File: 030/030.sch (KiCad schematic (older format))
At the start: 7 parts, among them J1 Conn_01x12, J2 USB_C_Receptacle_USB2.0

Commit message: update 030 to potentially correct schematic. Remove bad 001/011.
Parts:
- removed R3, R4: comp, Resistor_SMD:R_0603_1608Metric_Pad0.98x0.95mm_HandSolder, symbol Device:R
- D1: symbol MSL0104RGB:MSL0104RGB -> 030-rescue:MSL0104RGB-MSL0104RGB
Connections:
- net +5V: now also J1.5 (Pin_5), J1.6 (Pin_6); no longer D1.1 (R_Annode), D1.2 (G_Annode), D1.6 (B_Annode), D1.7 (R_Annode), J1.8 (Pin_8)
- net D+: now also J2.A6 (D+), J2.B6 (D+)
- net D-: now also J2.A7 (D-), J2.B7 (D-)
- new net Annode: D1.1 (R_Annode), D1.2 (G_Annode), D1.6 (B_Annode), D1.7 (R_Annode), J1.8 (Pin_8)
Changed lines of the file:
@@
 	2300 2150 2250 2150
 Connection ~ 2250 2150
-Text Label 1750 2150 3    50   ~ 0
-D+
-Text Label 1950 2150 3    50   ~ 0
-D-
 $Comp
 L power:+5V #PWR0104
@@
 L power:+5V #PWR0109
 U 1 1 62279281
-P 900 2400
-F 0 "#PWR0109" H 900 2250 50  0001 C CNN
-F 1 "+5V" V 915 2528 50  0000 L CNN
-F 2 "" H 900 2400 50  0001 C CNN
-F 3 "" H 900 2400 50  0001 C CNN
-	1    900  2400
+P 900 2650
+F 0 "#PWR0109" H 900 2500 50  0001 C CNN
+F 1 "+5V" V 915 2778 50  0000 L CNN
+F 2 "" H 900 2650 50  0001 C CNN
+F 3 "" H 900 2650 50  0001 C CNN
+	1    900  2650
 	0    1    1    0
 $EndComp
 Wire Wire Line
-	900  2600 900  2700
+	900  2600 900  2650
 Text Label 900  3000 0    50   ~ 0
 D+
@@
 Text Label 900  2100 0    50   ~ 0
 B
+Connection ~ 900  2650
+Wire Wire Line
+	900  2650 900  2700
+Text Label 900  2400 0    50   ~ 0
+Annode
+Text Label 2100 3050 1    50   ~ 0
+Annode
+Text Label 1600 3050 1    50   ~ 0
+Annode
+Text Label 1500 3050 1    50   ~ 0
+Annode
 $Comp
-L MSL0104RGB:MSL0104RGB D1
+L 030-rescue:MSL0104RGB-MSL0104RGB D1
 U 1 1 6226D102
 P 1800 3200
@@
 	-1   0    0    1
 $EndComp
-$Comp
-L power:+5V #PWR0110
-U 1 1 6226E87F
-P 1500 3050
-F 0 "#PWR0110" H 1500 2900 50  0001 C CNN
-F 1 "+5V" H 1515 3223 50  0000 C CNN
-F 2 "" H 1500 3050 50  0001 C CNN
-F 3 "" H 1500 3050 50  0001 C CNN
-	1    1500 3050
-	1    0    0    -1
-$EndComp
-$Comp
-L power:+5V #PWR0111
-U 1 1 6226F068
-P 2100 3050
-F 0 "#PWR0111" H 2100 2900 50  0001 C CNN
-F 1 "+5V" H 2115 3223 50  0000 C CNN
-F 2 "" H 2100 3050 50  0001 C CNN
-F 3 "" H 2100 3050 50  0001 C CNN
-	1    2100 3050
-	1    0    0    -1
-$EndComp
-$Comp
-L power:+5V #PWR0112
-U 1 1 6226F88D
-P 1600 3050
-F 0 "#PWR0112" H 1600 2900 50  0001 C CNN
-F 1 "+5V" H 1615 3223 50  0000 C CNN
-F 2 "" H 1600 3050 50  0001 C CNN
-F 3 "" H 1600 3050 50  0001 C CNN
-	1    1600 3050
-	1    0    0    -1
-$EndComp
-$Comp
-L power:+5V #PWR0113
-U 1 1 6226FB45
-P 2000 3050
-F 0 "#PWR0113" H 2000 2900 50  0001 C CNN
-F 1 "+5V" H 2015 3223 50  0000 C CNN
-F 2 "" H 2000 3050 50  0001 C CNN
-F 3 "" H 2000 3050 50  0001 C CNN
-	1    2000 3050
-	1    0    0    -1
-$EndComp
-Text Label 1700 3050 0    50   ~ 0
+Text Label 2000 3050 1    50   ~ 0
+Annode
+Text Label 1800 3050 1    50   ~ 0
+R
+Text Label 1700 3050 1    50   ~ 0
 B
-Text Label 1800 3050 0    50   ~ 0
-R
-Text Label 1900 3050 0    50   ~ 0
+Text Label 1750 1850 3    50   ~ 0
+D+
+Text Label 1950 1850 3    50   ~ 0
+D-
+Text Label 1900 3050 1    50   ~ 0
 G
-$Comp
-L Device:R R3
-U 1 1 62270907
-P 1750 2000
-F 0 "R3" V 1650 1950 50  0000 L CNN
-F 1 "comp" V 1750 1900 50  0000 L CNN
-F 2 "Resistor_SMD:R_0603_1608Metric_Pad0.98x0.95mm_HandSolder" V 1680 2000 50  0001 C CNN
-F 3 "~" H 1750 2000 50  0001 C CNN
-	1    1750 2000
-	1    0    0    -1
-$EndComp
-$Comp
-L Device:R R4
-U 1 1 62270BB0
-P 1950 2000
-F 0 "R4" V 1850 1950 50  0000 L CNN
-F 1 "comp" V 1950 1900 50  0000 L CNN
-F 2 "Resistor_SMD:R_0603_1608Metric_Pad0.98x0.95mm_HandSolder" V 1880 2000 50  0001 C CNN
-F 3 "~" H 1950 2000 50  0001 C CNN
-	1    1950 2000
-	1    0    0    -1
-$EndComp
 $EndSCHEMATC

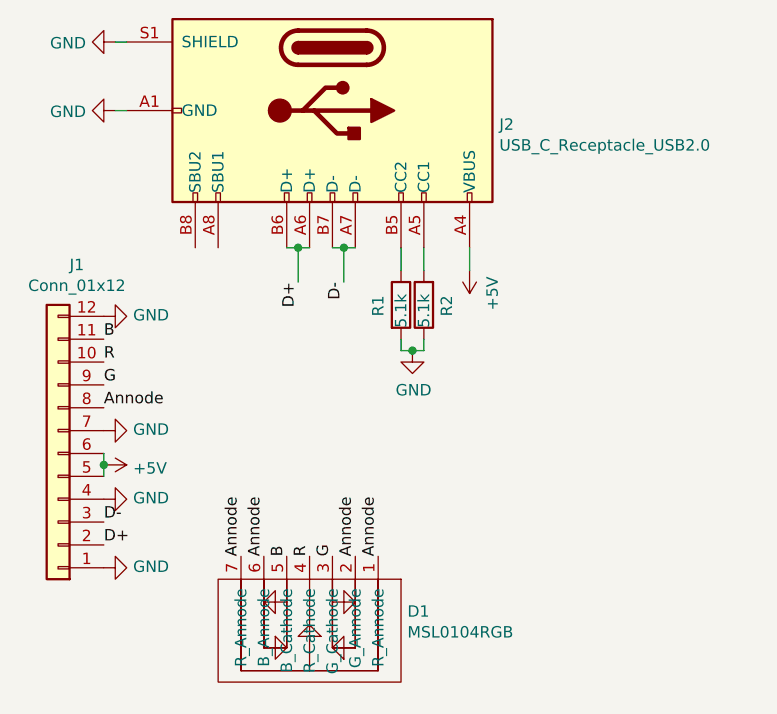
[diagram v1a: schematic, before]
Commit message: 001, 011, 030 standardized to a cheaper LED
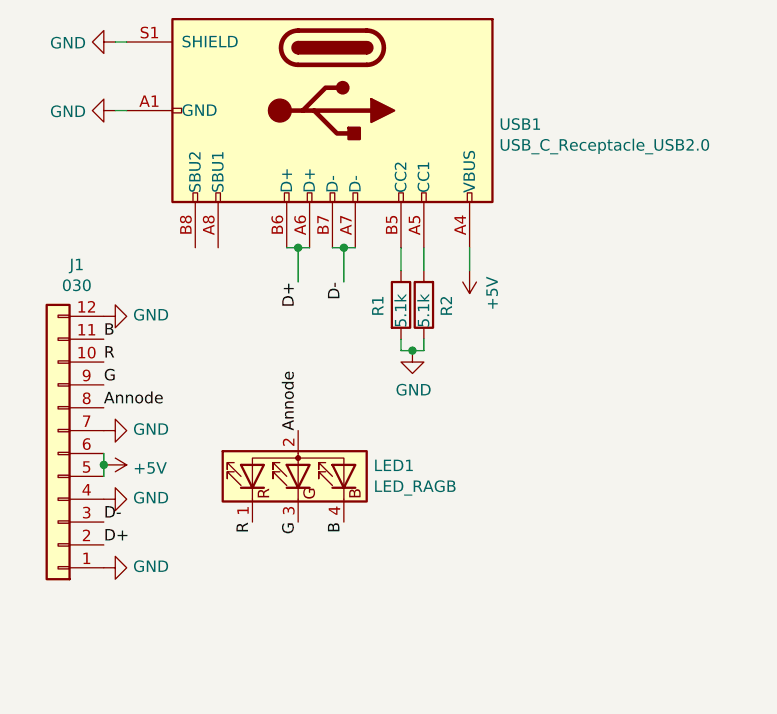
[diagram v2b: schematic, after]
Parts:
- removed D1: MSL0104RGB, MSL0104RGB:MSL0104RGB, symbol 030-rescue:MSL0104RGB-MSL0104RGB
- added LED1: LED_RAGB, New_LED:FM-3510RGBA-SG, symbol Device:LED_RAGB
- J1: value Conn_01x12 -> 030
- renumbered J2 to USB1
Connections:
- net Annode: now also LED1.2 (A)
- net B: now also LED1.4 (BK)
- net G: now also LED1.3 (GK)
- net R: now also LED1.1 (RK)
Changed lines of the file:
@@
 $EndDescr
 $Comp
-L Connector:USB_C_Receptacle_USB2.0 J2
+L Connector:USB_C_Receptacle_USB2.0 USB1
 U 1 1 6226C837
 P 1900 1100
-F 0 "J2" V 1961 1830 50  0000 L CNN
+F 0 "USB1" V 1961 1830 50  0000 L CNN
 F 1 "USB_C_Receptacle_USB2.0" V 2052 1830 50  0000 L CNN
 F 2 "Connector_USB:USB_C_Receptacle_HRO_TYPE-C-31-M-12" H 2050 1100 50  0001 C CNN
@@
 P 700 2600
 F 0 "J1" H 618 1775 50  0000 C CNN
-F 1 "Conn_01x12" H 618 1866 50  0000 C CNN
+F 1 "030" H 618 1866 50  0000 C CNN
 F 2 "Molex 5034801200:503480-1200" H 700 2600 50  0001 C CNN
 F 3 "~" H 700 2600 50  0001 C CNN
@@
 Text Label 900  2400 0    50   ~ 0
 Annode
-Text Label 2100 3050 1    50   ~ 0
+Text Label 1750 2500 1    50   ~ 0
 Annode
-Text Label 1600 3050 1    50   ~ 0
-Annode
-Text Label 1500 3050 1    50   ~ 0
-Annode
-$Comp
-L 030-rescue:MSL0104RGB-MSL0104RGB D1
-U 1 1 6226D102
-P 1800 3200
-F 0 "D1" H 1372 3291 50  0000 R CNN
-F 1 "MSL0104RGB" H 1372 3382 50  0000 R CNN
-F 2 "MSL0104RGB:MSL0104RGB" H 1800 3200 50  0001 C CNN
-F 3 "" H 1800 3200 50  0001 C CNN
-	1    1800 3200
-	-1   0    0    1
-$EndComp
-Text Label 2000 3050 1    50   ~ 0
-Annode
-Text Label 1800 3050 1    50   ~ 0
+Text Label 1550 2900 3    50   ~ 0
 R
-Text Label 1700 3050 1    50   ~ 0
+Text Label 1950 2900 3    50   ~ 0
 B
 Text Label 1750 1850 3    50   ~ 0
@@
 Text Label 1950 1850 3    50   ~ 0
 D-
-Text Label 1900 3050 1    50   ~ 0
+Text Label 1750 2900 3    50   ~ 0
 G
+$Comp
+L Device:LED_RAGB LED1
+U 1 1 625DCB12
+P 1750 2700
+F 0 "LED1" V 1796 2370 50  0000 R CNN
+F 1 "LED_RAGB" V 1705 2370 50  0000 R CNN
+F 2 "New_LED:FM-3510RGBA-SG" H 1750 2650 50  0001 C CNN
+F 3 "~" H 1750 2650 50  0001 C CNN
+	1    1750 2700
+	0    -1   -1   0
+$EndComp
 $EndSCHEMATC
